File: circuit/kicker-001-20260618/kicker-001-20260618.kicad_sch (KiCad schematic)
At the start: 16 parts, among them J1 Conn_Relay, J2 Conn_Solenoid_{Front}, J3 Conn_Solenoid_{Back}, Q1 NMOS, U2 74AHC1G04, U4 74AHC1G04, U6 74AHC1G04

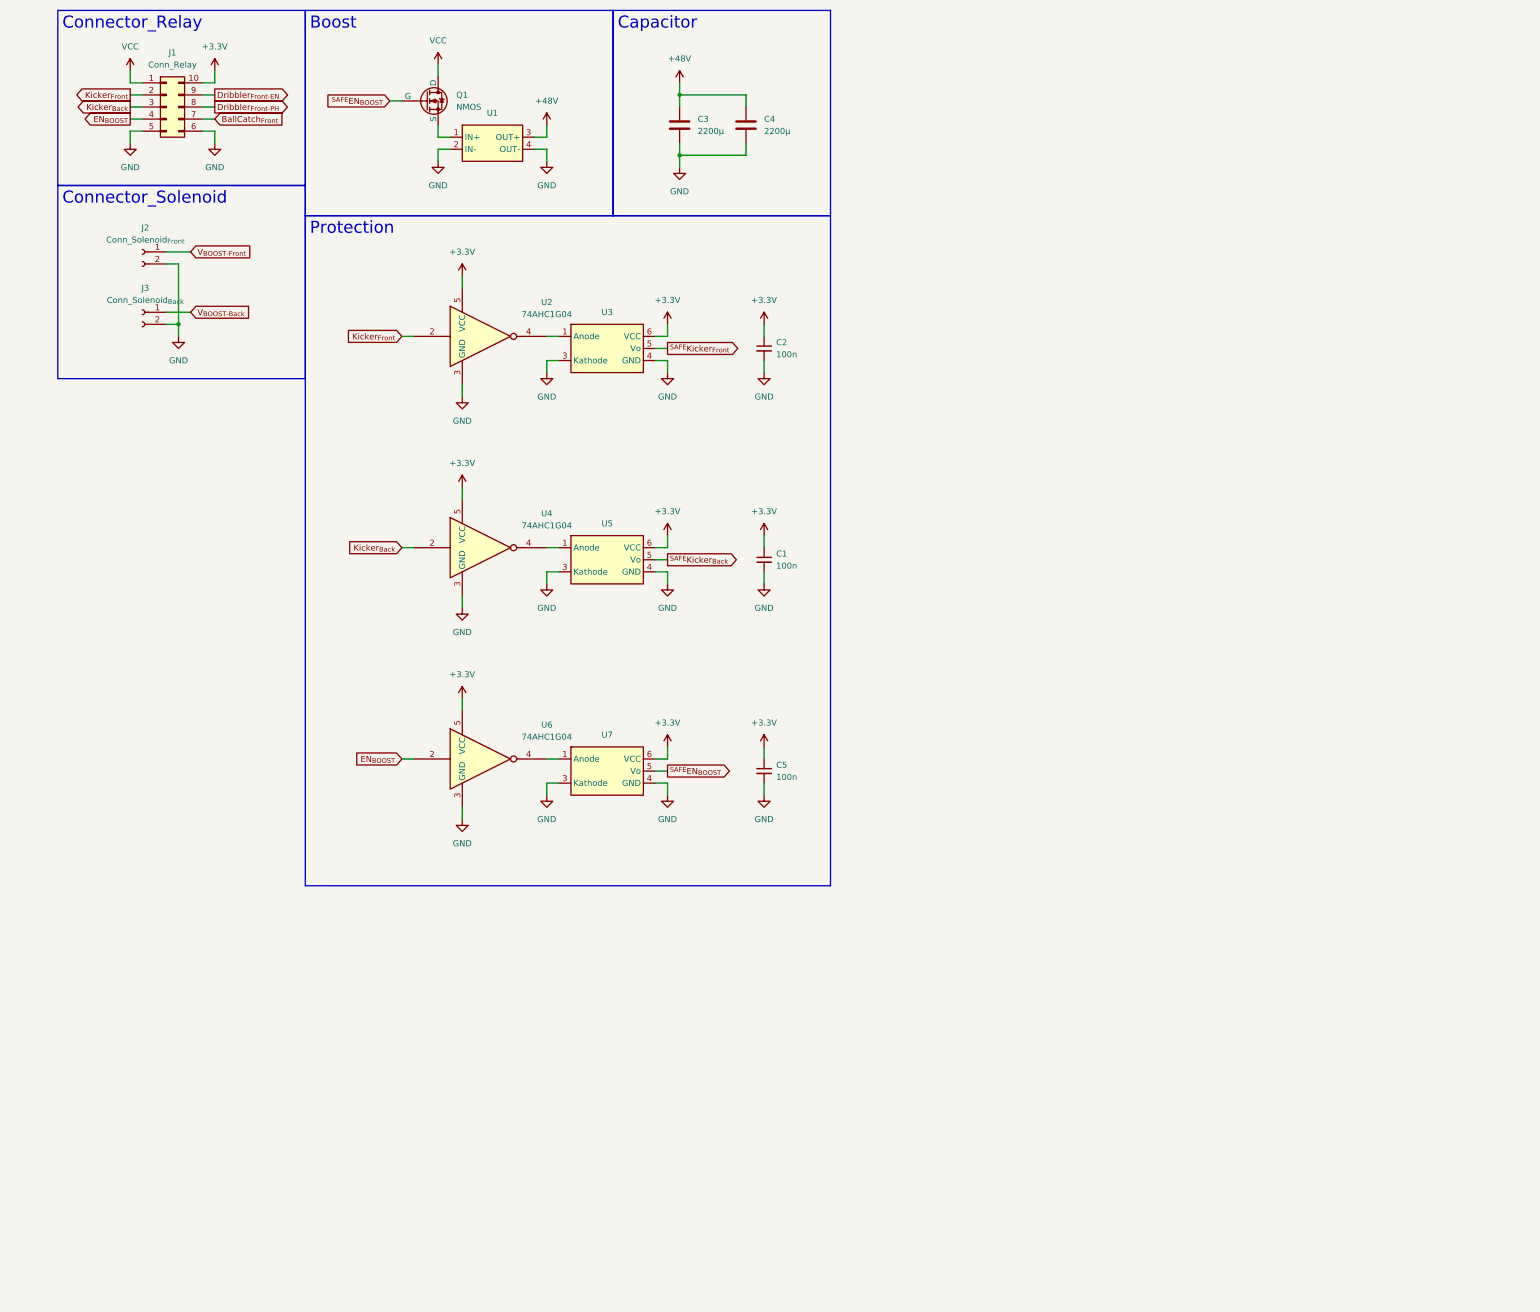
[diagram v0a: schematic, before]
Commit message: Update キッカー基板の回路図を完成させた
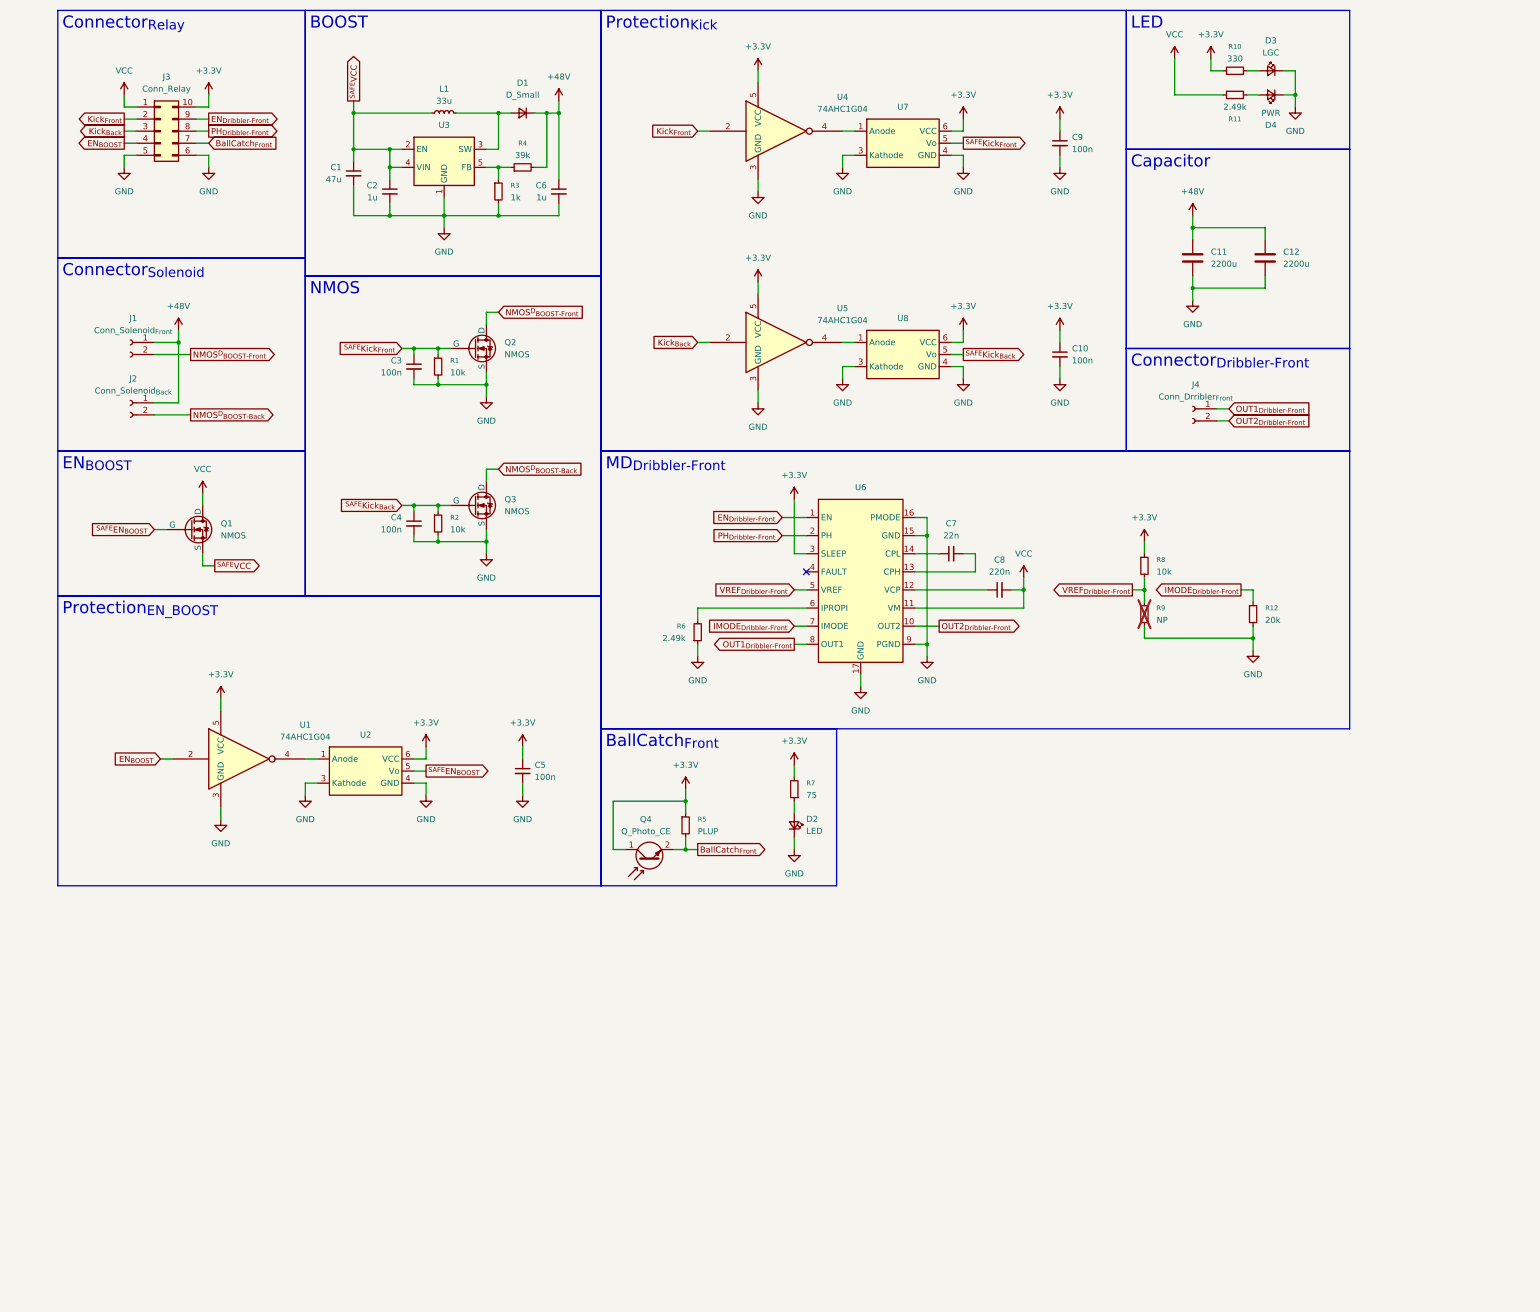
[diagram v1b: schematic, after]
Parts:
- removed C3, C4: 2200μ, symbol Device:C
- removed U1: (no value), symbol @Thrive_symbol_kicker:XL6009E1_Module
- added C1: 47u, symbol Device:C_Small
- added C11, C12: 2200u, symbol Device:C
- added C2, C6: 1u, symbol Device:C_Small
- added C3, C4: 100n, symbol Device:C_Small
- added C7: 22n, symbol Device:C_Small
- added C8: 220n, symbol Device:C_Small
- added D1: D_Small, symbol Device:D_Small
- added D2: LED, symbol Device:LED_Small
- added D3: LGC, symbol Device:LED_Small
- added D4: PWR, symbol Device:LED_Small
- added J4: Conn_Drribler_{Front}, symbol Connector:Conn_01x02_Socket
- added L1: 33u, symbol Device:L_Small
- added Q2, Q3: NMOS, symbol Simulation_SPICE:NMOS
- added Q4: Q_Photo_CE, symbol Device:Q_Photo_NPN_CE
- added R1, R2: 10k, symbol Device:R_Small
- added R10: 330, symbol Device:R_Small
- added R11, R6: 2.49k, symbol Device:R_Small
- added R12: 20k, Resistor_SMD:R_0603_1608Metric, symbol Device:R_Small
- added R3: 1k, symbol Device:R_Small
- added R4: 39k, symbol Device:R_Small
- added R5: PLUP, symbol Device:R_Small
- added R7: 75, symbol Device:R_Small
- added R8: 10k, Resistor_SMD:R_0603_1608Metric, symbol Device:R_Small
- added R9: NP, Resistor_SMD:R_0603_1608Metric, symbol Device:R_Small
- added U3: (no value), Package_TO_SOT_SMD:TO-263-5_TabPin3, symbol @Thrive_symbol_kicker:XL6009E1
- added U6: (no value), symbol @Thrive_symbol_kicker:DRV8874
- renumbered C1 to C10, C2 to C9, J2 to J1, J3 to J2, J1 to J3, U6 to U1, U7 to U2, U2 to U4, U4 to U5, U3 to U7, U5 to U8
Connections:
- net V_{BOOST-Back} is gone; now on net +48V: J2.1 (Pin_1)
- net V_{BOOST-Front} is gone; now on net +48V: J1.1 (Pin_1)
- net +3.3V: now also Q4.1 (C), R10.1, R5.1, R7.2, R8.1, U6.3 (SLEEP)
- net +48V: now also C11.1, C12.1, C6.1, D1.1 (K), R4.2
- net BallCatch_{Front}: now also Q4.2 (E), R5.2
- net GND: now also C1.2, C11.2, C12.2, C2.2, C3.2, C4.2, C6.2, D2.1 (K), D3.1 (K), D4.1 (K), Q2.3 (S), Q3.3 (S), R1.2, R12.2, R2.2, R3.2, R6.1, R9.2, U3.1 (GND), U6.15 (GND), U6.16 (PMODE), U6.17 (GND), U6.9 (PGND); no longer J1.2 (Pin_2), J2.2 (Pin_2)
- net VCC: now also C8.2, R11.1, U6.11 (VM)
- net ^{SAFE}VCC: now reaches Q1.3 (S)
- net ^{SAFE}VCC: now also C1.1, C2.1, L1.1, U3.2 (EN), U3.4 (VIN)
- net Dribbler_{Front-EN} renamed EN_{Dribbler-Front}
- net EN_{Dribbler-Front}: now also U6.1 (EN)
- net Dribbler_{Front-PH} renamed PH_{Dribbler-Front}
- net PH_{Dribbler-Front}: now also U6.2 (PH)
- net Kicker_{Back} renamed Kick_{Back}
- net Kicker_{Front} renamed Kick_{Front}
- net ^{SAFE}Kicker_{Back} renamed ^{SAFE}Kick_{Back}
- net ^{SAFE}Kick_{Back}: now also C4.1, Q3.2 (G), R2.1
- net ^{SAFE}Kicker_{Front} renamed ^{SAFE}Kick_{Front}
- net ^{SAFE}Kick_{Front}: now also C3.1, Q2.2 (G), R1.1
- new net: D1.2 (A), L1.2, U3.3 (SW)
- new net: C8.1, U6.12 (VCP)
- new net: C7.2, U6.13 (CPH)
- new net: C7.1, U6.14 (CPL)
- new net: R6.2, U6.6 (IPROPI)
- new net: R3.1, R4.1, U3.5 (FB)
- new net: D4.2 (A), R11.2
- new net: D2.2 (A), R7.1
- new net: D3.2 (A), R10.2
- new net IMODE_{Dribbler-Front}: R12.1, U6.7 (IMODE)
- new net NMOS^{D}_{BOOST-Back}: J2.2 (Pin_2), Q3.1 (D)
- new net NMOS^{D}_{BOOST-Front}: J1.2 (Pin_2), Q2.1 (D)
- new net OUT1_{Dribbler-Front}: J4.1 (Pin_1), U6.8 (OUT1)
- new net OUT2_{Dribbler-Front}: J4.2 (Pin_2), U6.10 (OUT2)
- new net VREF_{Dribbler-Front}: R8.2, R9.1, U6.5 (VREF)
- no-connect marks 0 -> 1
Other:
- moved on the sheet: C10, C5, C9, J1, J2, J3, Q1, U1, U2, U4, U5, U7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

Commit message: Update キッカー基板のDRを受けて修正
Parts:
- added C10, C9: 1000u, symbol Device:C
- added Q2: PMOS, symbol Simulation_SPICE:PMOS
- added R1: 100, symbol Device:R_Small
- added R2, R3: 10k, symbol Device:R_Small
- C7: renamed from C11; value 2200u -> 1000u
- C8: renamed from C12; value 2200u -> 1000u
- R4: renamed from R5; value PLUP -> 10k
- R9: renamed from R4; value 39k -> 36k
- U2, U7, U8: value (none) -> TLP2361
- U6: value (none) -> DRV8874
- renumbered C7 to C11, C8 to C12, C9 to C13, C10 to C14, D2 to D1, D1 to D2, J4 to J3, J3 to J4, Q4 to Q3, Q2 to Q4, Q3 to Q5, R6 to R10, R8 to R11, R9 to R12, R12 to R13, R10 to R14, R11 to R15, R1 to R5, R2 to R6, R3 to R7, R7 to R8
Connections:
- net +3.3V: no longer R4.1
- net +48V: now also C10.1, C9.1
- net BallCatch_{Front}: now also R4.1; no longer R4.2
- net GND: now also Q1.3 (S), R4.2, C10.2, C9.2, R2.1
- net VCC: now also Q2.1 (D), R3.1; no longer Q1.1 (D)
- net ^{SAFE}EN_{BOOST}: now also R1.1; no longer Q1.2 (G)
- net ^{SAFE}VCC: now also Q2.3 (S); no longer Q1.3 (S)
- new net: Q1.1 (D), Q2.2 (G), R3.2
- new net: Q1.2 (G), R1.2, R2.2
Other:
- moved on the sheet: C11, C12, C5, C7, C8, D1, J3, Q1, Q3, R10, R11, R12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

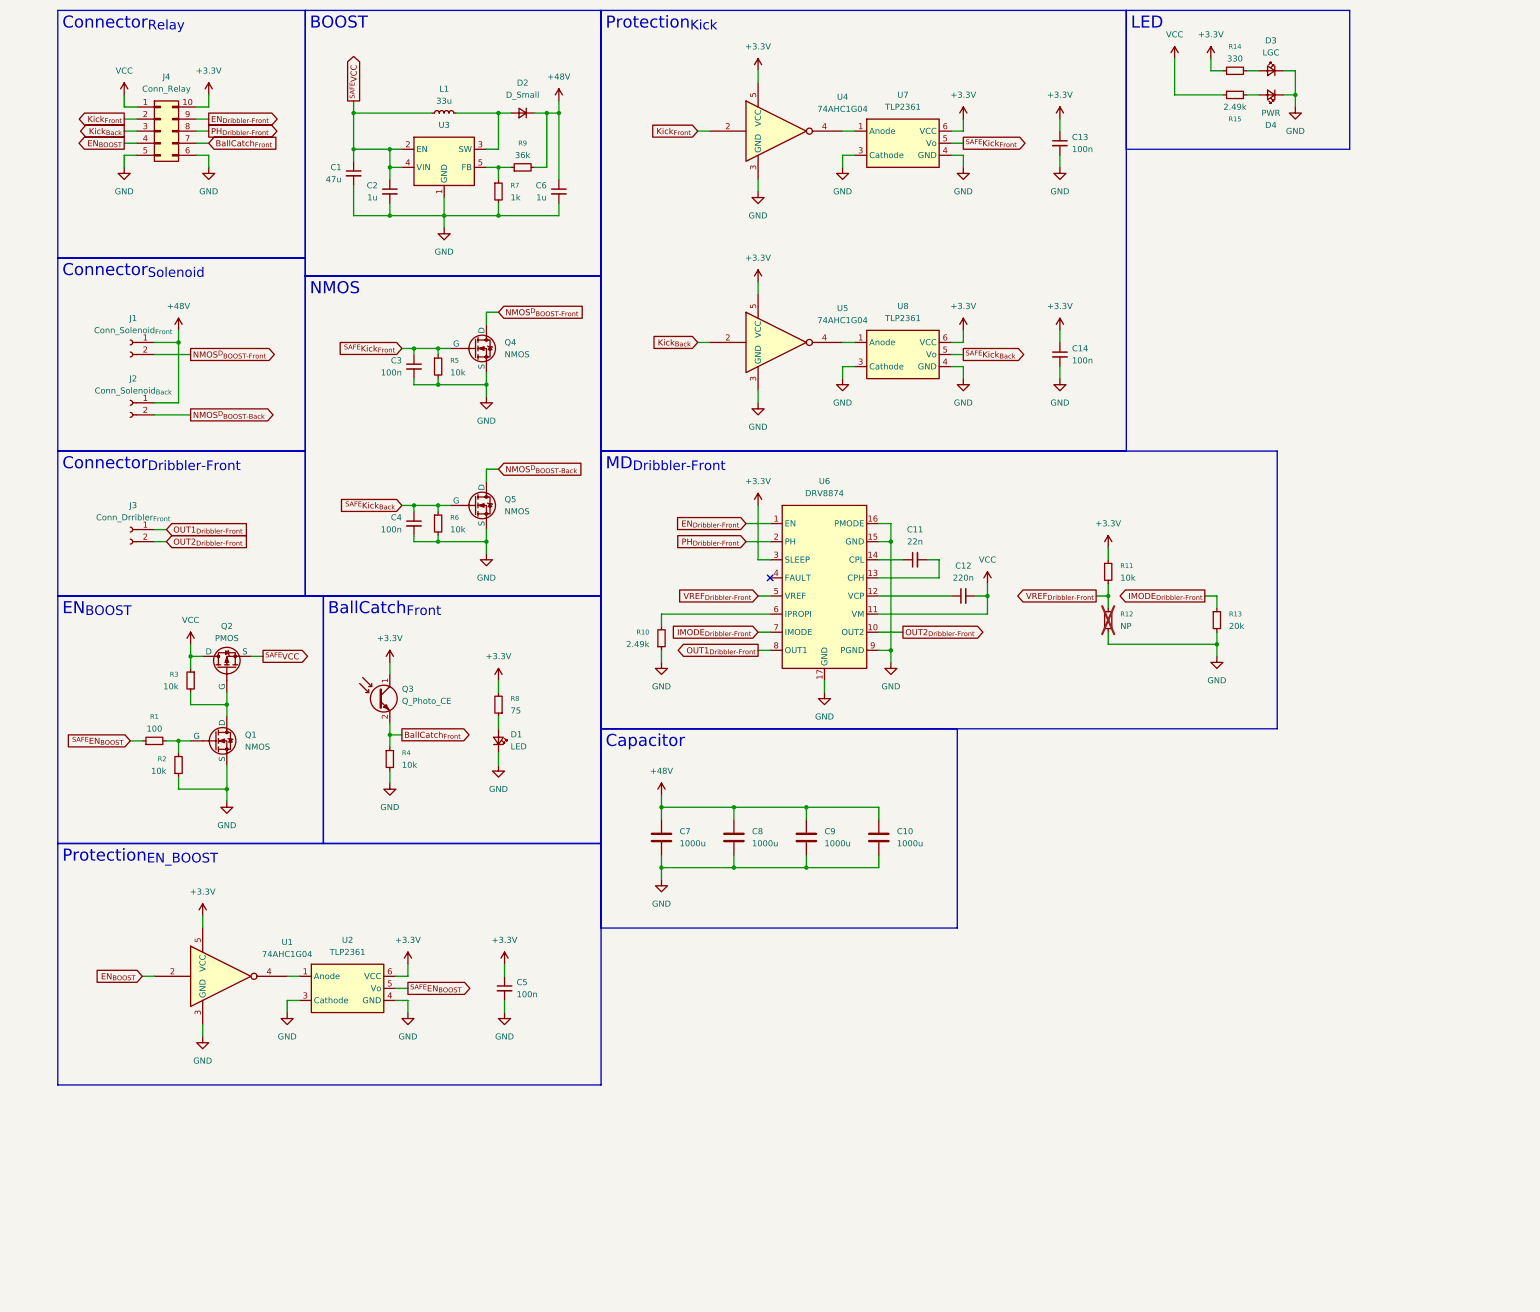
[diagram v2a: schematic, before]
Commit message: Update キッカー基板の回路図をDRに基づいて更新
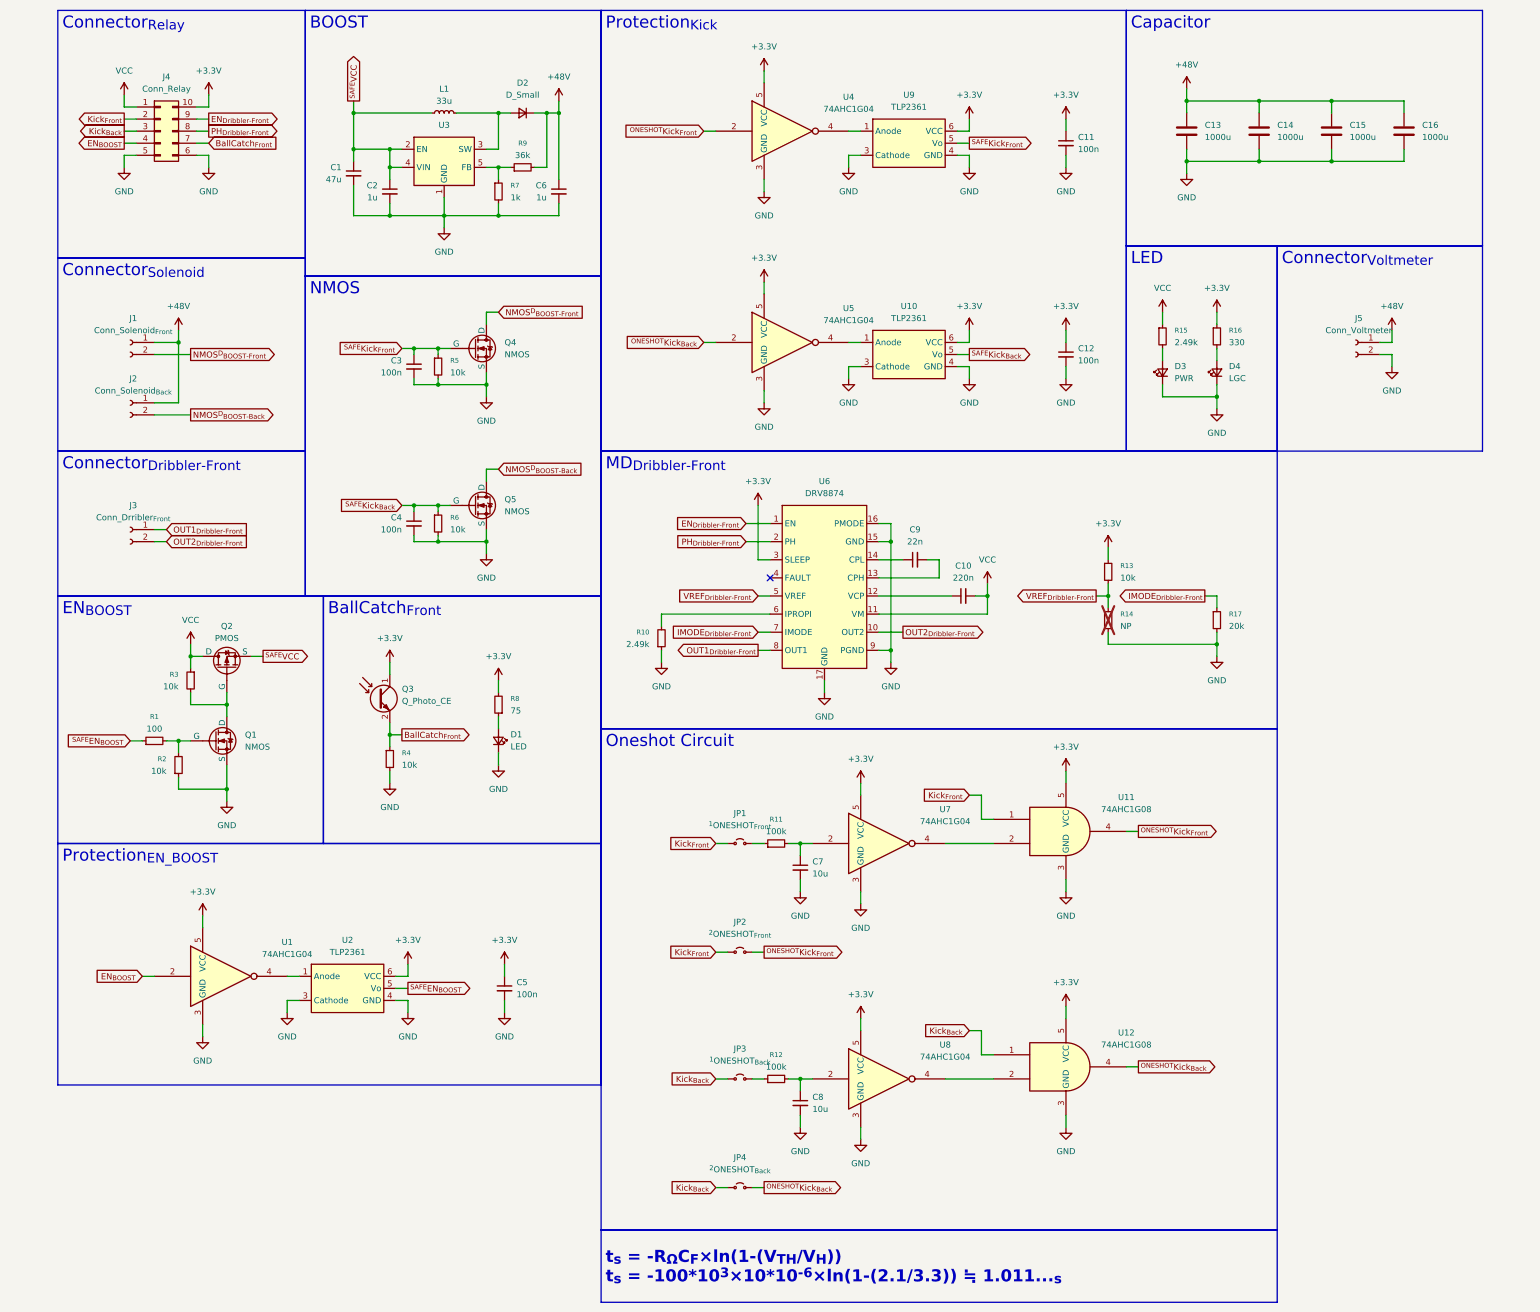
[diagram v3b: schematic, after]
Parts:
- removed R14: 330, symbol Device:R_Small
- added C7, C8: 10u, symbol Device:C_Small
- added J5: Conn_Voltmeter, symbol Connector:Conn_01x02_Socket
- added JP1: ^{1}ONESHOT_{Front}, symbol Jumper:Jumper_2_Small_Open
- added JP2: ^{2}ONESHOT_{Front}, symbol Jumper:Jumper_2_Small_Open
- added JP3: ^{1}ONESHOT_{Back}, symbol Jumper:Jumper_2_Small_Open
- added JP4: ^{2}ONESHOT_{Back}, symbol Jumper:Jumper_2_Small_Open
- added R11, R12: 100k, symbol Device:R_Small
- added R16: 330, symbol Device:R_Small
- added U11, U12: 74AHC1G08, symbol 74xGxx:74AHC1G08
- added U7, U8: 74AHC1G04, symbol 74xGxx:74AHC1G04
- D3: value LGC -> PWR
- D4: value PWR -> LGC
- renumbered C12 to C10, C13 to C11, C14 to C12, C7 to C13, C8 to C14, C9 to C15, C10 to C16, C11 to C9, R11 to R13, R12 to R14, R13 to R17, U8 to U10, U7 to U9
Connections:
- net +3.3V: now also R16.1, U11.5 (VCC), U12.5 (VCC), U7.5 (VCC), U8.5 (VCC)
- net +48V: now also J5.1 (Pin_1)
- net GND: now also C7.2, C8.2, J5.2 (Pin_2), U11.3 (GND), U12.3 (GND), U7.3 (GND), U8.3 (GND)
- net Kick_{Back}: now also JP3.1 (A), JP4.1 (A), U12.1; no longer U5.2
- net Kick_{Front}: now also JP1.1 (A), JP2.1 (A), U11.1; no longer U4.2
- net at R15.2: now also D3.2 (A); no longer D4.2 (A)
- new net: U12.2, U8.4
- new net: C7.1, R11.2, U7.2
- new net: U11.2, U7.4
- new net: JP1.2 (B), R11.1
- new net: JP3.2 (B), R12.1
- new net: C8.1, R12.2, U8.2
- new net: D4.2 (A), R16.2
- new net ^{ONESHOT}Kick_{Back}: JP4.2 (B), U12.4, U5.2
- new net ^{ONESHOT}Kick_{Front}: JP2.2 (B), U11.4, U4.2
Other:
- moved on the sheet: C11, C12, C13, C14, C15, C16, U10, U4, U5, U9
